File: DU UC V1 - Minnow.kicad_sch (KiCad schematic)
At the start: 1 part

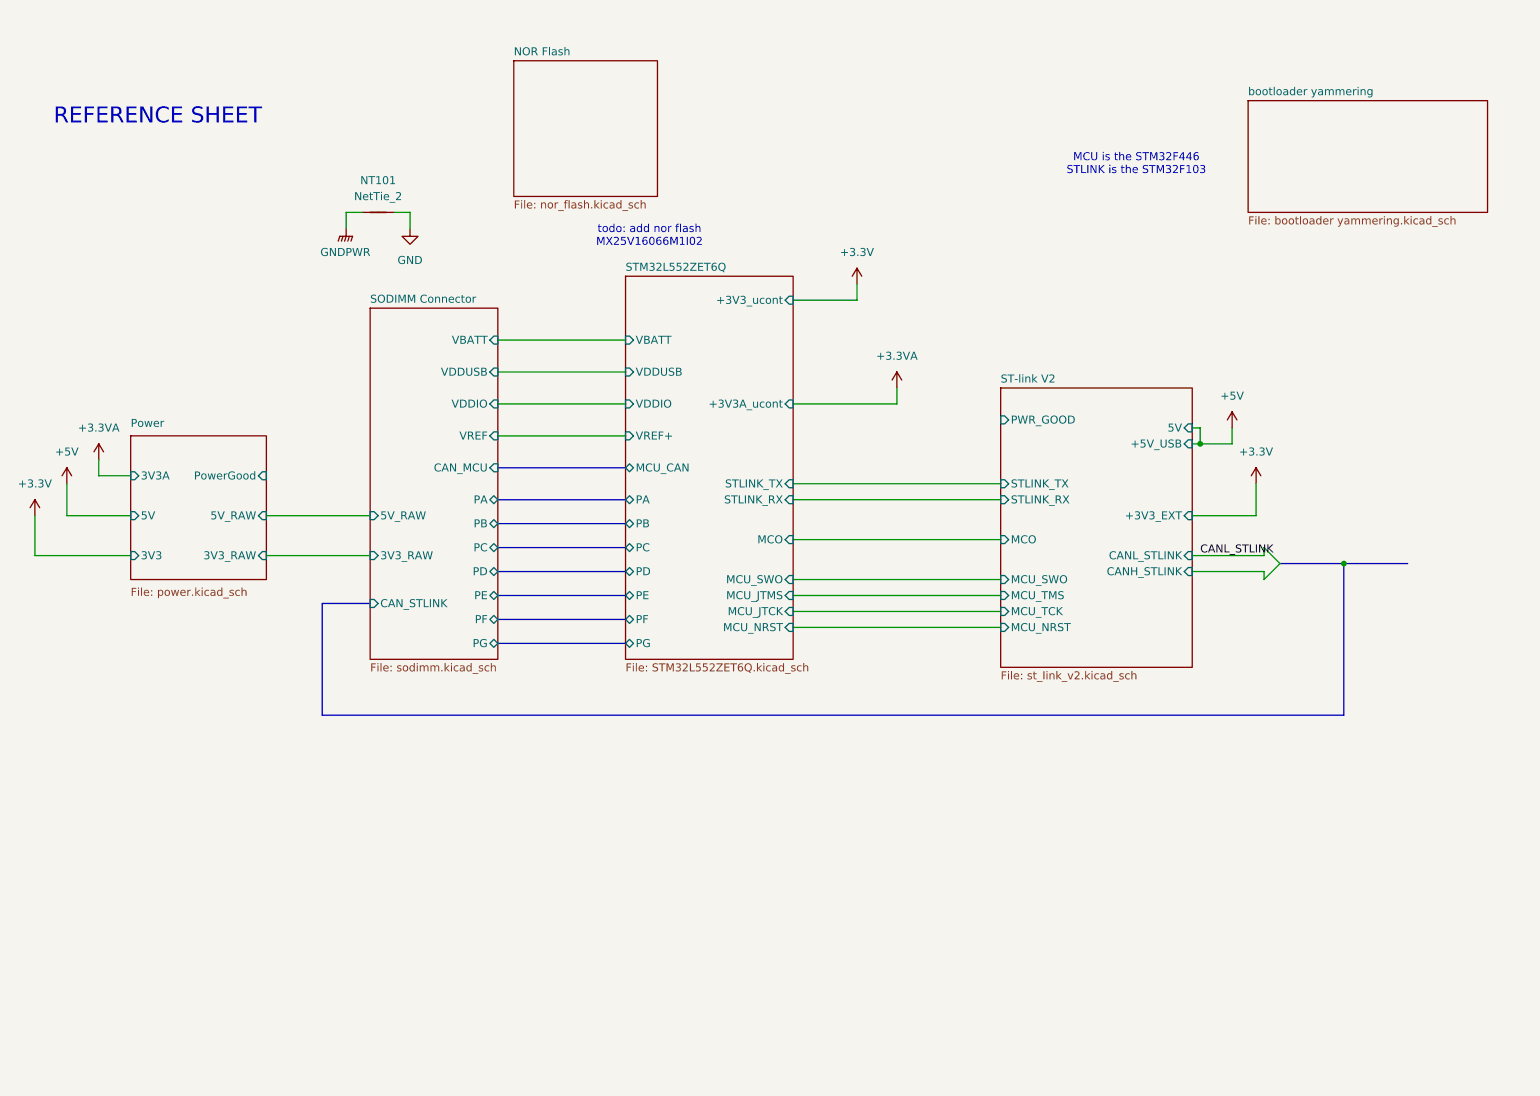
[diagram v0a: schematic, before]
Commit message: jk im stupid forgot to route the flash
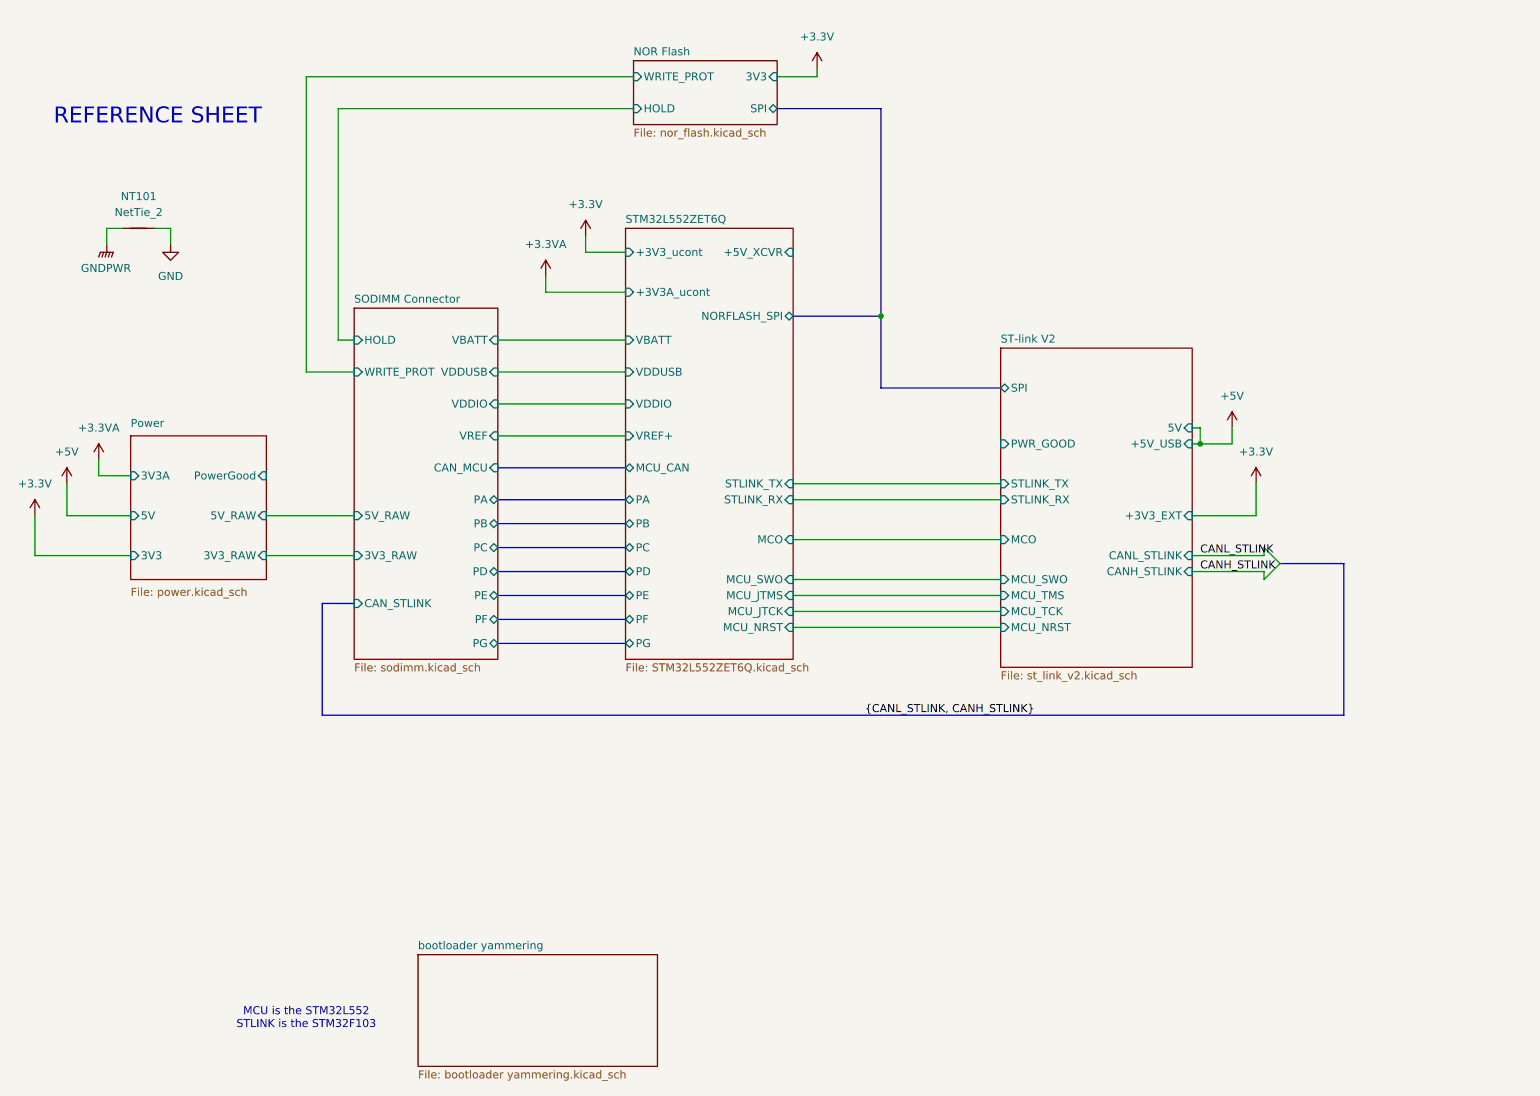
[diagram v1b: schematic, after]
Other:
- sheet NOR Flash ports: added 3V3, HOLD, SPI, WRITE_PROT; removed none
- sheet SODIMM Connector ports: added HOLD, WRITE_PROT; removed none
- sheet ST-link V2 ports: added SPI; removed none
- sheet STM32L552ZET6Q ports: added +5V_XCVR, NORFLASH_SPI; removed none
- note added: "MCU is the STM32L552 STLINK is the STM32F103"
- note removed: "MCU is the STM32F446 STLINK is the STM32F103"
- note removed: "todo: add nor flash MX25V16066M1I02"
- moved on the sheet: NT101

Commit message: fixed like a bunch of things, power and new xcvr and lights and other goodies, also started layout
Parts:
- NT101: footprint (none) -> NetTie:NetTie-2_SMD_Pad2.0mm
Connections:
- no-connect marks 0 -> 1
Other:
- added sheet Debug LED Array (ledarray.kicad_sch)
- sheet Power ports: added 3V3A_RAW; removed 3V3_RAW, 5V, PowerGood
- sheet SODIMM Connector ports: added +5V, 3V3A; removed 3V3_RAW, 5V_RAW
- sheet ST-link V2 ports: added none; removed 5V
- sheet STM32L552ZET6Q ports: added LED_ARR_DATA; removed +5V_XCVR
- note added: "SPI is NC here because used to want to connect this to flash module but lowkey the stlink shouldn't need more memory at all"
- note added: "todo: double check stlink"

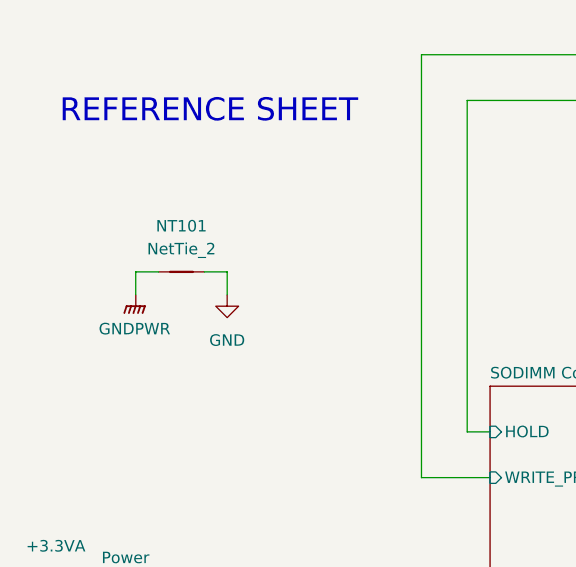
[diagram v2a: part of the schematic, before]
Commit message: laid out most of power, main xcvr, prob some other stuff
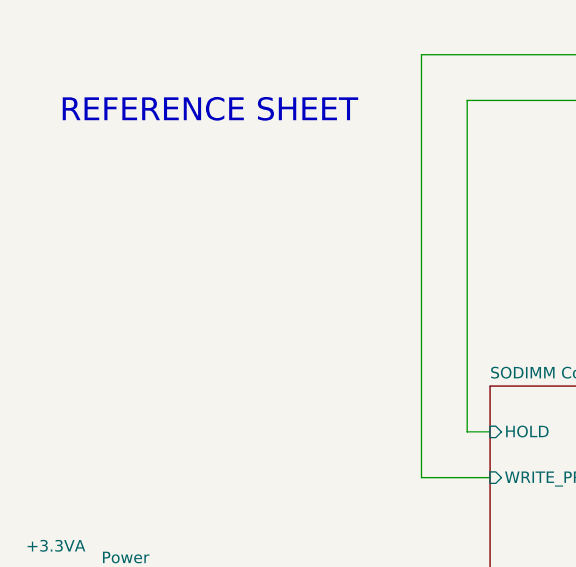
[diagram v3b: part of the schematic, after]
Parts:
- removed NT101: NetTie_2, NetTie:NetTie-2_SMD_Pad2.0mm, symbol Device:NetTie_2
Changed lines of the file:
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@@
-	(wire
-		(pts
-			(xy 48.26 52.07) (xy 50.8 52.07)
-		)
-		(stroke
-			(width 0)
-			(type default)
-		)
-	)
 	(wire
 		(pts
@@
 	(wire
 		(pts
-			(xy 55.88 52.07) (xy 58.42 52.07)
-		)
-		(stroke
-			(width 0)
-			(type default)
-		)
-	)
-	(wire
-		(pts
 			(xy 232.41 104.14) (xy 220.98 104.14)
 		)
@@
 		)
 	)
-	(wire
-		(pts
-			(xy 58.42 52.07) (xy 58.42 54.61)
-		)
-		(stroke
-			(width 0)
-			(type default)
-		)
-	)
 	(bus
 		(pts
@@
 		(pts
 			(xy 154.94 33.02) (xy 171.45 33.02)
-		)
-		(stroke
-			(width 0)
-			(type default)
-		)
-	)
-	(wire
-		(pts
-			(xy 48.26 54.61) (xy 48.26 52.07)
 		)
 		(stroke
@@
 					(unit 1)
 				)
-			)
-		)
-	)
-	(symbol
-		(lib_id "power:GND")
-		(at 58.42 54.61 0)
-		(unit 1)
-		(exclude_from_sim no)
-		(in_bom yes)
-		(on_board yes)
-		(dnp no)
-		(fields_autoplaced yes)
-		(property "Reference" "#PWR0104"
-			(at 58.42 60.96 0)
-			(effects
-				(font
-					(size 1.27 1.27)
-				)
-				(hide yes)
-			)
-		)
-		(property "Value" "GND"
-			(at 58.42 59.69 0)
-			(effects
-				(font
-					(size 1.27 1.27)
-				)
-			)
-		)
-		(property "Footprint" ""
-			(at 58.42 54.61 0)
-			(effects
-				(font
-					(size 1.27 1.27)
-				)
-				(hide yes)
-			)
-		)
-		(property "Datasheet" ""
-			(at 58.42 54.61 0)
-			(effects
-				(font
-					(size 1.27 1.27)
-				)
-				(hide yes)
-			)
-		)
-		(property "Description" "Power symbol creates a global label with name \"GND\" , ground"
-			(at 58.42 54.61 0)
-			(effects
-				(font
-					(size 1.27 1.27)
-				)
-				(hide yes)
-			)
-		)
-		(pin "1"
-		)
-		(instances
-			(project "DU UC V1 - Minnow"
-				(path "/0aeff2df-21bc-4c76-95d6-83ff8577a8db"
-					(reference "#PWR0104")
-					(unit 1)
-				)
-			)
-		)
-	)
-	(symbol
-		(lib_id "Device:NetTie_2")
-		(at 53.34 52.07 0)
-		(unit 1)
-		(exclude_from_sim no)
-		(in_bom no)
-		(on_board yes)
-		(dnp no)
-		(fields_autoplaced yes)
-		(property "Reference" "NT101"
-			(at 53.34 46.99 0)
-			(effects
-				(font
-					(size 1.27 1.27)
-				)
-			)
-		)
-		(property "Value" "NetTie_2"
-			(at 53.34 49.53 0)
-			(effects
-				(font
-					(size 1.27 1.27)
-				)
-			)
-		)
-		(property "Footprint" "NetTie:NetTie-2_SMD_Pad2.0mm"
-			(at 53.34 52.07 0)
-			(effects
-				(font
-					(size 1.27 1.27)
-				)
-				(hide yes)
-			)
-		)
-		(property "Datasheet" "~"
-			(at 53.34 52.07 0)
-			(effects
-				(font
-					(size 1.27 1.27)
-				)
-				(hide yes)
-			)
-		)
-		(property "Description" "Net tie, 2 pins"
-			(at 53.34 52.07 0)
-			(effects
-				(font
-					(size 1.27 1.27)
-				)
-				(hide yes)
-			)
-		)
-		(pin "1"
-		)
-		(pin "2"
-		)
-		(instances
-			(project "DU UC V1 - Minnow"
-				(path "/0aeff2df-21bc-4c76-95d6-83ff8577a8db"
-					(reference "NT101")
-					(unit 1)
-				)
-			)
-		)
-	)
-	(symbol
-		(lib_id "power:GNDPWR")
-		(at 48.26 54.61 0)
-		(unit 1)
-		(exclude_from_sim no)
-		(in_bom yes)
-		(on_board yes)
-		(dnp no)
-		(fields_autoplaced yes)
-		(property "Reference" "#PWR0103"
-			(at 48.26 59.69 0)
-			(effects
-				(font
-					(size 1.27 1.27)
-				)
-				(hide yes)
-			)
-		)
-		(property "Value" "GNDPWR"
-			(at 48.133 58.42 0)
-			(effects
-				(font
-					(size 1.27 1.27)
-				)
-			)
-		)
-		(property "Footprint" ""
-			(at 48.26 55.88 0)
-			(effects
-				(font
-					(size 1.27 1.27)
-				)
-				(hide yes)
-			)
-		)
-		(property "Datasheet" ""
-			(at 48.26 55.88 0)
-			(effects
-				(font
-					(size 1.27 1.27)
-				)
-				(hide yes)
-			)
-		)
-		(property "Description" "Power symbol creates a global label with name \"GNDPWR\" , global ground"
-			(at 48.26 54.61 0)
-			(effects
-				(font
-					(size 1.27 1.27)
-				)
-				(hide yes)
-			)
-		)
-		(pin "1"
-		)
-		(instances
-			(project "DU UC V1 - Minnow"
-				(path "/0aeff2df-21bc-4c76-95d6-83ff8577a8db"
-					(reference "#PWR0103")
-					(unit 1)
-				)

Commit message: i fucken rerouted everything and redid the pinout like 3x, half routed GPIOs
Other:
- sheet ST-link V2 ports: added STLINK_CAN+, STLINK_CAN-; removed CANH_STLINK, CANL_STLINK
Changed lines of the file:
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@@
 		)
 	)
-	(label "{CANL_STLINK, CANH_STLINK}"
+	(label "{STLINK_CAN-, STLINK_CAN+}"
 		(at 168.91 129.54 0)
 		(effects
@@
 		)
 	)
-	(label "CANH_STLINK"
+	(label "STLINK_CAN+"
 		(at 222.25 106.68 0)
 		(effects
@@
 		)
 	)
-	(label "CANL_STLINK"
+	(label "STLINK_CAN-"
 		(at 222.25 104.14 0)
 		(effects
@@
 			)
 		)
-		(pin "CANL_STLINK" input
-			(at 220.98 104.14 0)
-			(effects
-				(font
-					(size 1.27 1.27)
-				)
-				(justify right)
-			)
-		)
-		(pin "CANH_STLINK" input
-			(at 220.98 106.68 0)
-			(effects
-				(font
-					(size 1.27 1.27)
-				)
-				(justify right)
-			)
-		)
 		(pin "MCU_SWO" input
 			(at 190.5 107.95 180)
@@
 			)
 		)
+		(pin "STLINK_CAN+" input
+			(at 220.98 106.68 0)
+			(effects
+				(font
+					(size 1.27 1.27)
+				)
+				(justify right)
+			)
+		)
+		(pin "STLINK_CAN-" input
+			(at 220.98 104.14 0)
+			(effects
+				(font
+					(size 1.27 1.27)
+				)
+				(justify right)
+			)
+		)

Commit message: small schematic changes, need to reroute
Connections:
- no-connect marks 1 -> 3
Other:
- sheet ST-link V2 ports: added MCU_NJRST; removed MCU_NRST
- sheet STM32L552ZET6Q ports: added MCU_NJRST; removed none
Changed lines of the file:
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@@
+	)
+	(no_connect
+		(at 157.48 83.82)
 	)
 	(no_connect
 		(at 190.5 77.47)
+	)
+	(no_connect
+		(at 190.5 86.36)
 	)
 	(bus_entry
@@
 	(wire
 		(pts
+			(xy 157.48 115.57) (xy 190.5 115.57)
+		)
+		(stroke
+			(width 0)
+			(type default)
+		)
+	)
+	(wire
+		(pts
 			(xy 39.37 90.17) (xy 44.45 90.17)
 		)
@@
 		(pts
 			(xy 245.11 129.54) (xy 82.55 129.54)
-		)
-		(stroke
-			(width 0)
-			(type default)
-		)
-	)
-	(wire
-		(pts
-			(xy 157.48 115.57) (xy 190.5 115.57)
 		)
 		(stroke
@@
 			)
 		)
-		(pin "MCU_NRST" input
+		(pin "MCU_NJRST" input
 			(at 190.5 115.57 180)
 			(effects
@@
 		)
 		(pin "MCU_NRST" input
-			(at 157.48 115.57 0)
+			(at 157.48 83.82 0)
 			(effects
 				(font
@@
 			)
 		)
+		(pin "MCU_NJRST" input
+			(at 157.48 115.57 0)
+			(effects
+				(font
+					(size 1.27 1.27)
+				)
+				(justify right)
+			)
+		)
